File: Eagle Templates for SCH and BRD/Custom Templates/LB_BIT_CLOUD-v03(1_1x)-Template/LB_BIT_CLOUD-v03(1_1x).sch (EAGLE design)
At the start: 16 parts, among them J2 BITSNAP_V03_MALE, J3 BITSNAP_V03_FEMALE, U1 LV321SOT23-5, U2 LV321SOT23-5

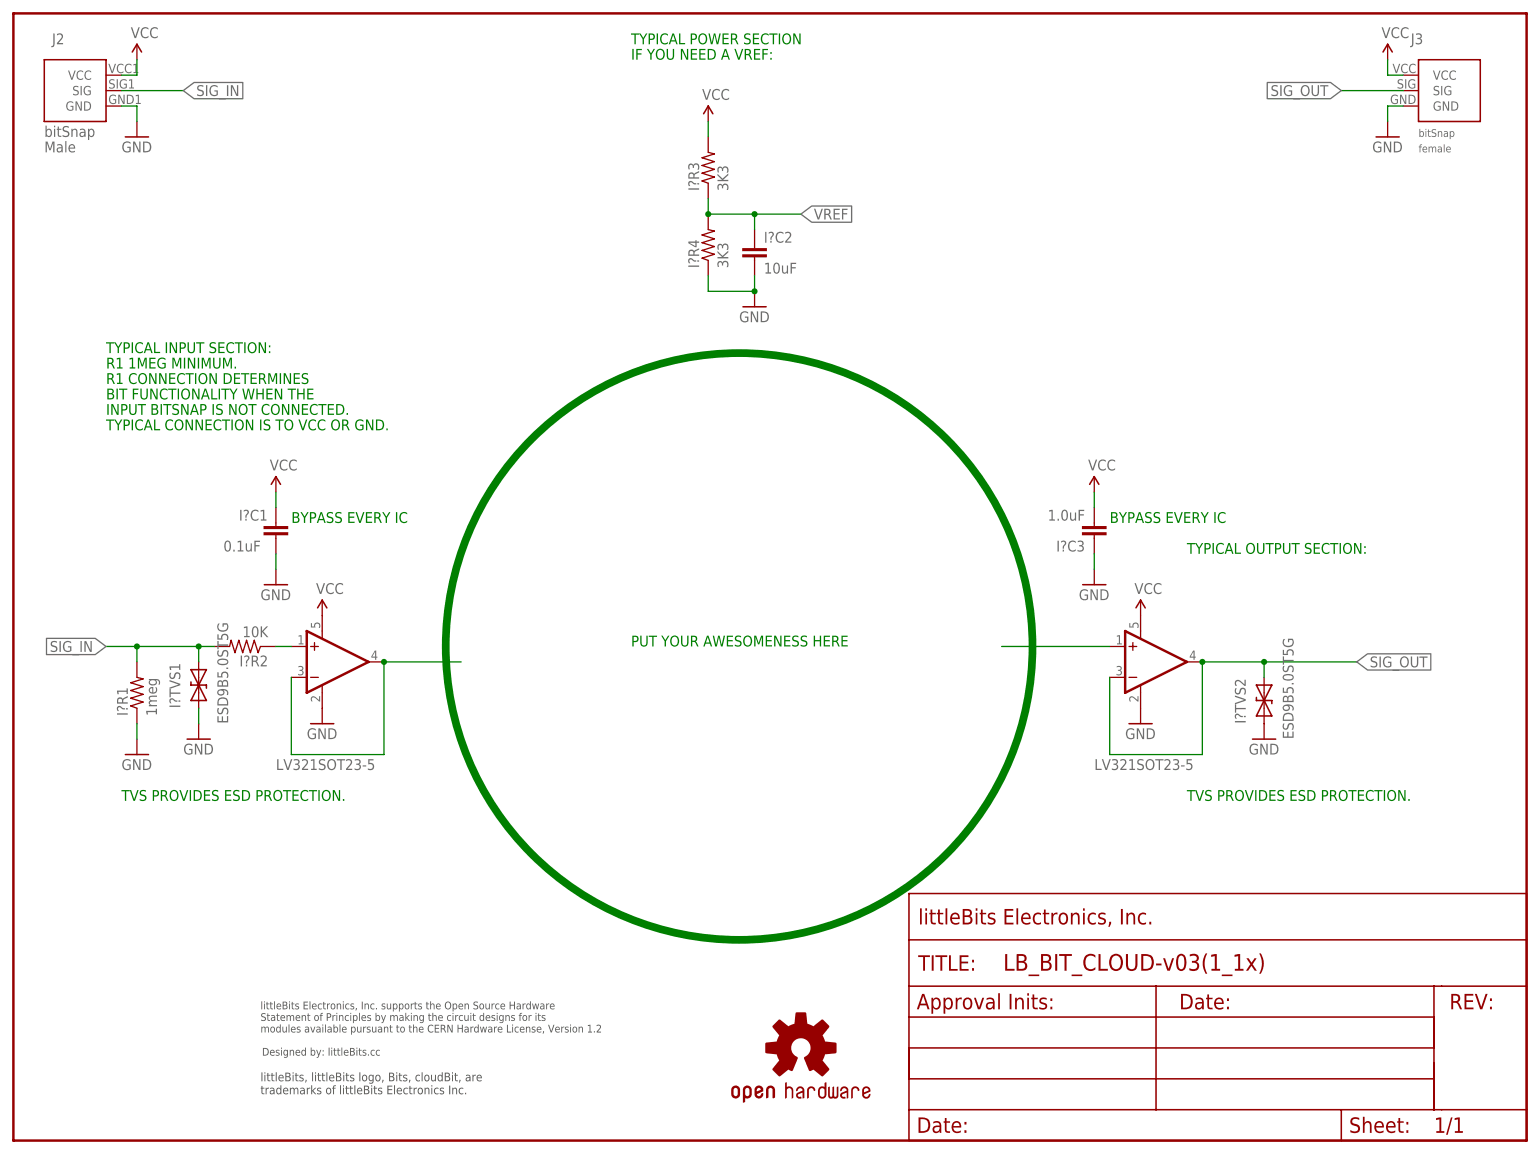
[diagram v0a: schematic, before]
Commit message: Updated templates
- Added ferrite beads
- Moved text and annotations off of Nets layer
- Minor layout changes
- Removed I/O/W prefix from reference designators
- Removed output stage components from output bits
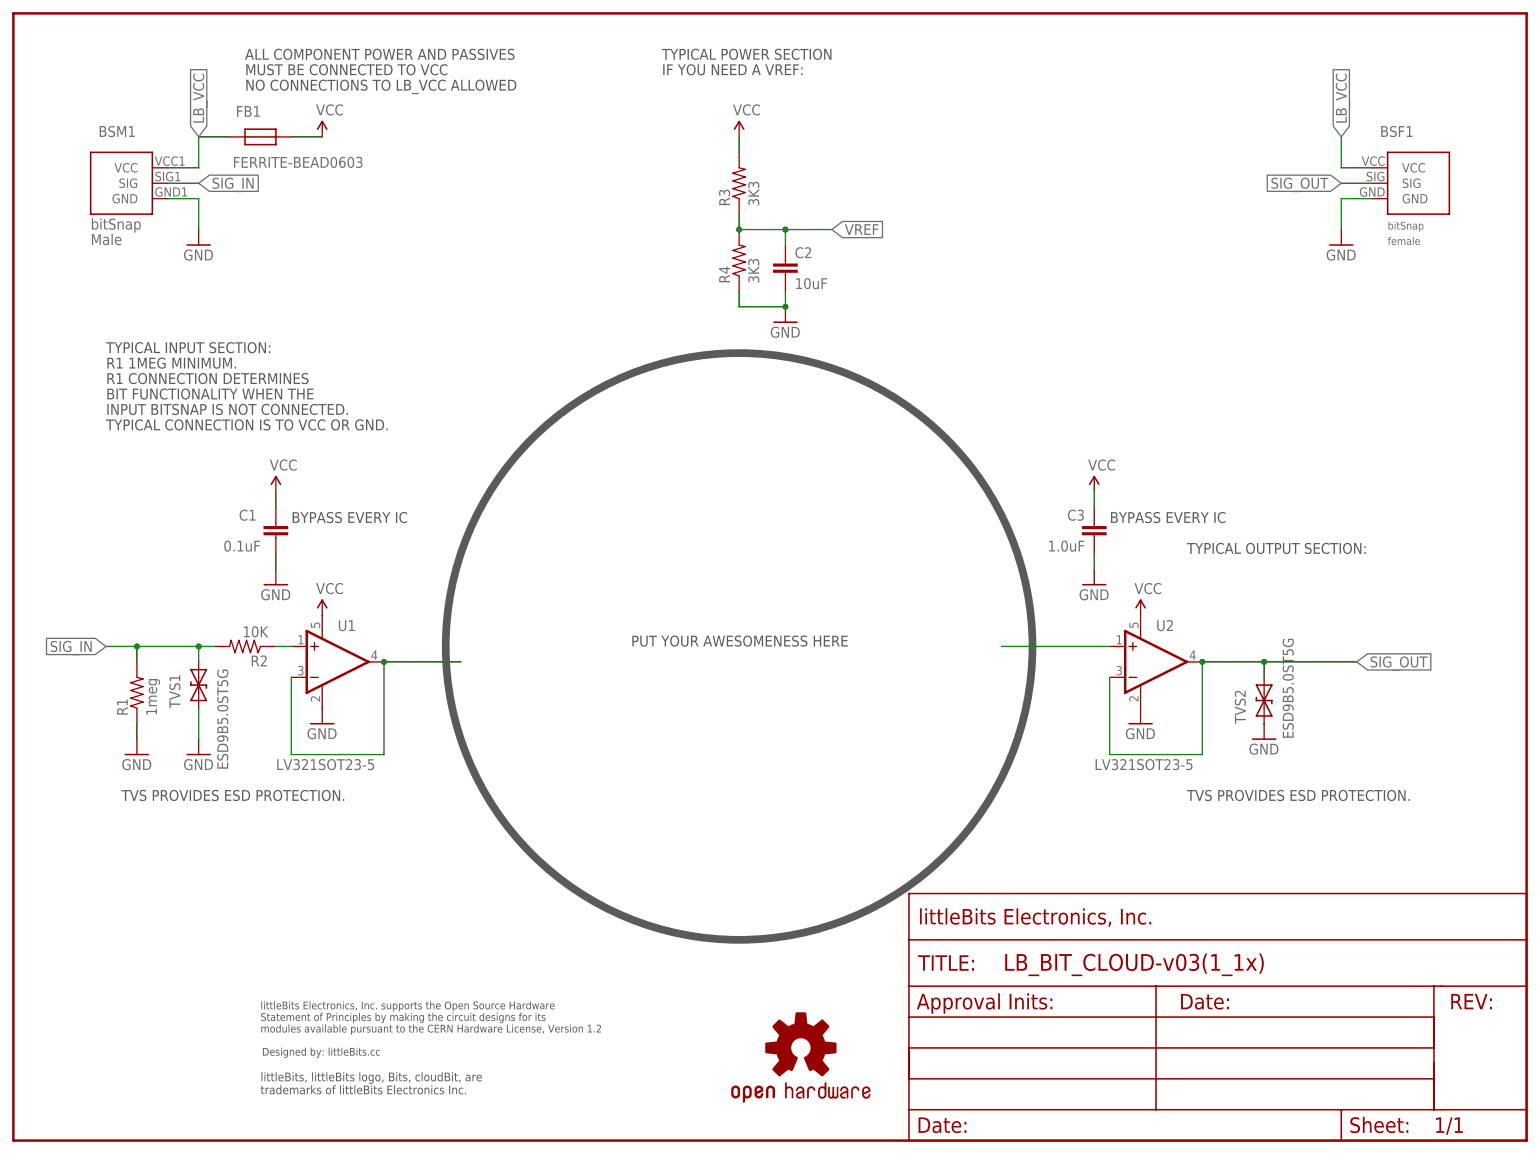
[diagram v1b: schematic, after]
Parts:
- removed I?C2: 10uF, LITTLEBITS:CAPCAP-0603
- removed I?R3, I?R4: 3K3, LITTLEBITS:RESISTOR0603
- removed J2: BITSNAP_V03_MALE, bitSnap:BITSNAP_V03_MALE
- removed J3: BITSNAP_V03_FEMALE, bitSnap:BITSNAP_V03_FEMALE
- added BSF1: BITSNAP_V03_FEMALE, bitSnap:BITSNAP_V03_FEMALE
- added BSM1: BITSNAP_V03_MALE, bitSnap:BITSNAP_V03_MALE
- added C2: 10uF, LITTLEBITS:CAPCAP-0603
- added FB1: FERRITE-BEAD0603, LITTLEBITS:FERRITE-BEAD0603
- added R3, R4: 3K3, LITTLEBITS:RESISTOR0603
- renumbered I?C1 to C1, I?C3 to C3, I?R1 to R1, I?R2 to R2, I?TVS1 to TVS1, I?TVS2 to TVS2
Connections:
- new net LB_VCC: BSF1.VCC, BSM1.VCC, FB1.P$2
- net GND: now also BSF1.GND, BSM1.GND, C2.2, R4.1; no longer I?C2.2, I?R4.1, J2.GND, J3.GND
- net SIG_IN: now also BSM1.SIG; no longer J2.SIG
- net SIG_OUT: now also BSF1.SIG; no longer J3.SIG
- net VCC: now also FB1.P$1, R3.2; no longer I?R3.2, J2.VCC, J3.VCC
- net VREF: now also C2.1, R3.1, R4.2; no longer I?C2.1, I?R3.1, I?R4.2
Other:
- note added: "ALL COMPONENT POWER AND PASSIVES"
- note added: "MUST BE CONNECTED TO VCC"
- note added: "NO CONNECTIONS TO LB_VCC ALLOWED"
